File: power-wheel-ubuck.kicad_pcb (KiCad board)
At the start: 2 copper layers, 23 parts, among them J1 CONN_01X02_MALE, J10 TEST_1P, J2 TEST_1P, J3 TEST_1P, J4 CONN_01X03_MALE, J5 TEST_1P, J6 TEST_1P, J7 TEST_1P, J8 TEST_1P, J9 CONN_01X02_MALE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

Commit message: Initial layout start
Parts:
- removed J10: TEST_1P, Measurement_Points:Measurement_Point_Square-SMD-Pad_Big
- moved C2 42.4 mm to (137.2, 90.2)
- moved J5 36.1 mm to (195.2, 110.6)
- moved J6 36.1 mm to (188.7, 110.6)
- moved R2 36.1 mm to (207.5, 114.9)
- moved J2 30.7 mm to (130.8, 81.3)
- moved C3 30.0 mm to (137.2, 94.0)
- moved C1 28.1 mm to (137.2, 86.4)
- moved J8 24.8 mm to (161.3, 81.3)
- moved C6 22.2 mm to (154.9, 90.2)
- moved J3 19.1 mm to (143.5, 81.3)
- moved C5 16.6 mm to (154.9, 94.0)
- moved R1 16.6 mm to (188.1, 101.3)
- moved C7 14.2 mm to (154.9, 86.4)
- moved J4 13.5 mm to (143.5, 107.3), turned to 180 degrees
- moved C4 12.8 mm to (156.4, 124.6)
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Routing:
- net Net-(C1-Pad1): track 0.00 -> 28.8 mm
- net GND: track 0.00 -> 21.6 mm
- added copper zone on F.Cu, net GND
- added copper zone on F.Cu, net Net-(C1-Pad1)
- added copper zone on F.Cu, net Net-(C5-Pad2)

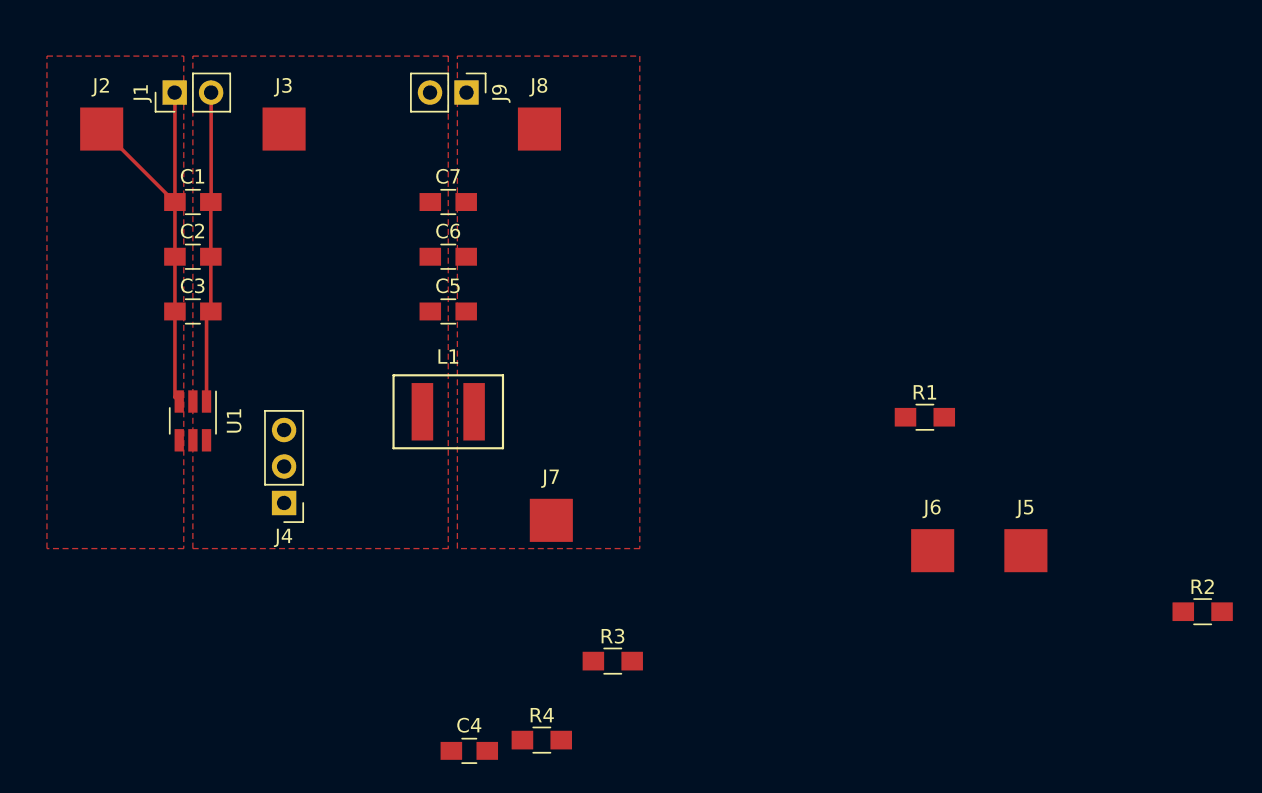
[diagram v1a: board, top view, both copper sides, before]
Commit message: First attempt at layout, needs tightening up
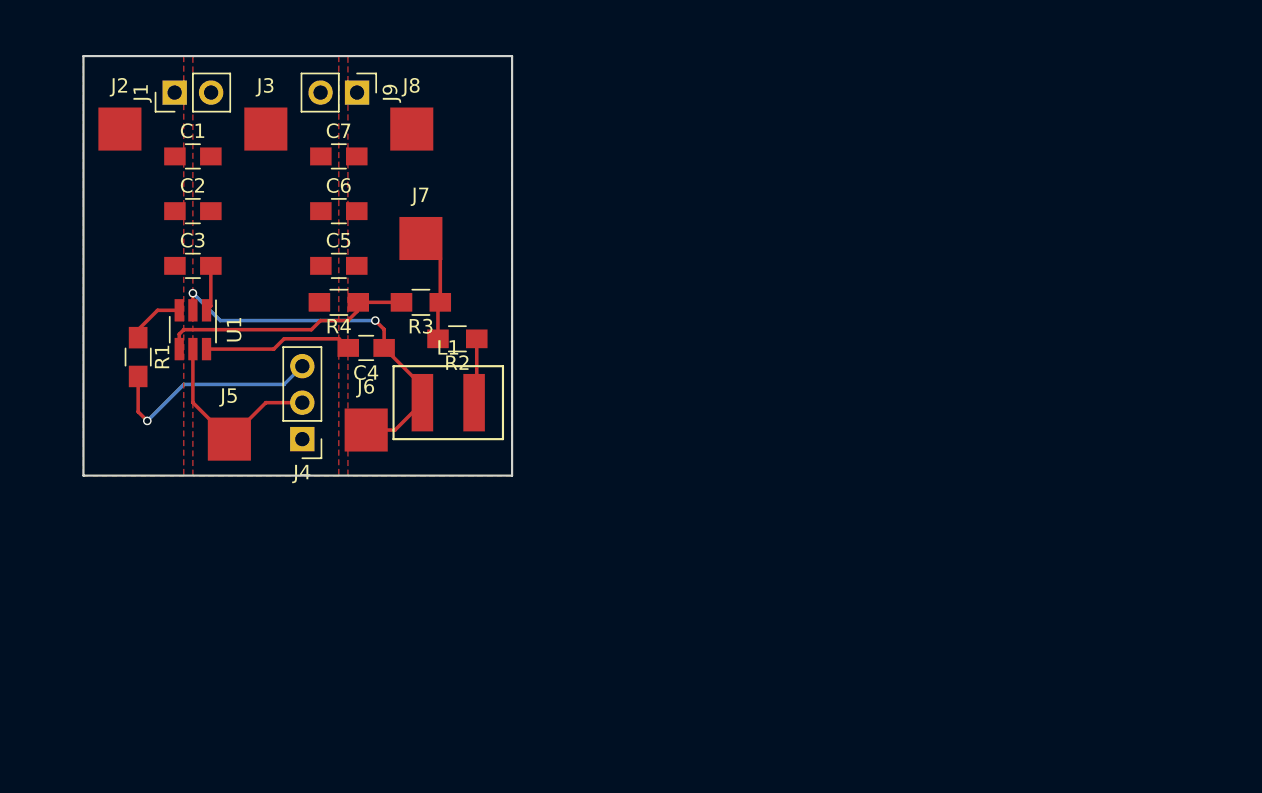
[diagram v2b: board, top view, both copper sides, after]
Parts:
- moved J5 56.0 mm to (139.7, 102.9)
- moved R2 55.3 mm to (155.6, 95.9), turned to 180 degrees
- moved R1 54.9 mm to (133.3, 97.2), turned to 270 degrees
- moved J6 40.3 mm to (149.2, 102.2)
- moved R4 33.6 mm to (147.3, 93.3), turned to 180 degrees
- moved C4 29.0 mm to (149.2, 96.5), turned to 180 degrees
- moved R3 28.3 mm to (153.0, 93.3), turned to 180 degrees
- moved J7 21.6 mm to (153.0, 88.9)
- moved J8 8.89 mm to (152.4, 81.3)
- moved C5 8.26 mm to (147.3, 90.8)
- moved C6 8.26 mm to (147.3, 87.0)
- moved C7 8.26 mm to (147.3, 83.2)
- moved J9 7.62 mm to (148.6, 78.7)
- moved U1 6.35 mm to (137.2, 95.2)
- moved J4 4.62 mm to (144.8, 102.9)
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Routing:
- net Net-(C4-Pad1): track 0.00 -> 26.5 mm, vias 0 -> 2
- net Net-(C1-Pad1): track 28.8 -> 4.02 mm
- net GND: track 21.6 -> 3.25 mm
- net Net-(R3-Pad2): track 0.00 -> 17.7 mm
- net Net-(J4-Pad3): track 0.00 -> 15.7 mm, vias 0 -> 1
- net Net-(J4-Pad2): track 0.00 -> 13.5 mm
- net Net-(C4-Pad2): track 0.00 -> 10.4 mm
- net Net-(J7-Pad1): track 0.00 -> 7.61 mm
- net Net-(C5-Pad2): track 0.00 -> 4.52 mm
- added copper zone on B.Cu, net GND
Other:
- board outline added: 29.8 x 29.2 mm

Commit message: Smaller test pad points
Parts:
- J2, J3, J5, J6, J7, J8: footprint Measurement_Points:Measurement_Point_Square-SMD-Pad_Big -> Measurement_Points:Measurement_Point_Square-SMD-Pad_Small

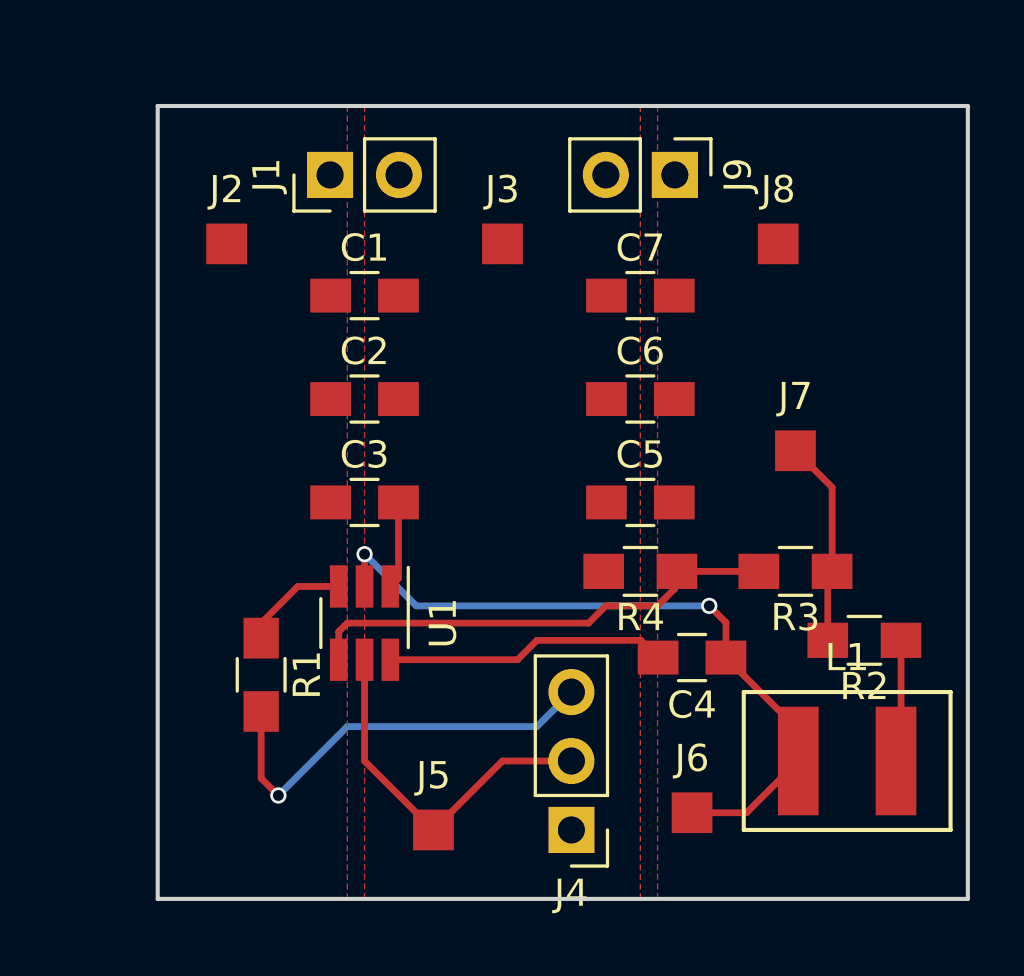
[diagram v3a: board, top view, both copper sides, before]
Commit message: Tightened up the layout
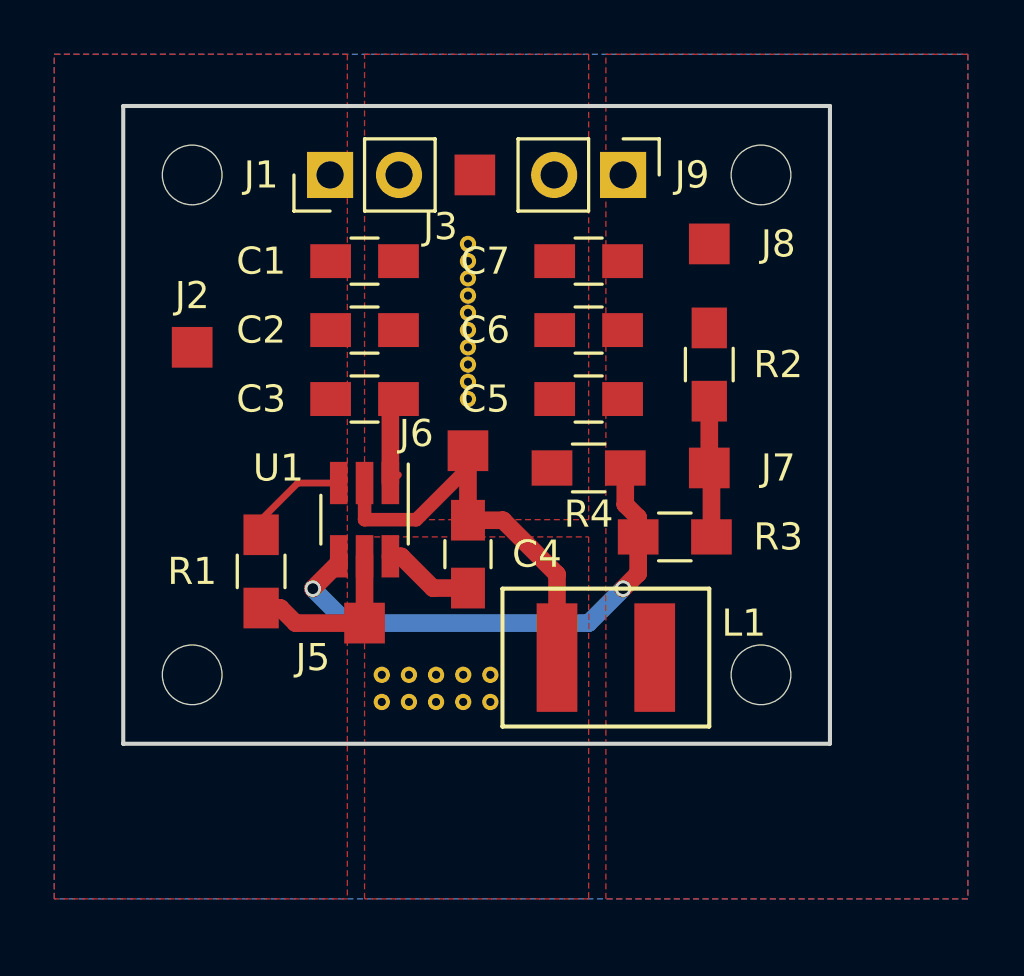
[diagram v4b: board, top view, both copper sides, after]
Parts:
- removed J4: CONN_01X03_MALE, Pin_Headers:Pin_Header_Straight_1x03_Pitch2.54mm
- added REF**: MountingHole_2.2mm_M2, Mounting_Holes:MountingHole_2.2mm_M2, F.Cu at (151.8, 97.2)
- added REF**: VIA-0.6mm, Extras:VIA-0.6mm, F.Cu at (141.0, 83.2)
- added REF**: VIA-0.6mm, Extras:VIA-0.6mm, F.Cu at (141.0, 82.5)
- added REF**: VIA-0.6mm, Extras:VIA-0.6mm, F.Cu at (141.0, 81.9)
- added REF**: VIA-0.6mm, Extras:VIA-0.6mm, F.Cu at (141.0, 81.3)
- added REF**: VIA-0.6mm, Extras:VIA-0.6mm, F.Cu at (141.8, 98.2)
- added REF**: VIA-0.6mm, Extras:VIA-0.6mm, F.Cu at (140.8, 98.2)
- added REF**: VIA-0.6mm, Extras:VIA-0.6mm, F.Cu at (139.8, 98.2)
- added REF**: VIA-0.6mm, Extras:VIA-0.6mm, F.Cu at (138.8, 98.2)
- added REF**: VIA-0.6mm, Extras:VIA-0.6mm, F.Cu at (137.8, 98.2)
- added REF**: VIA-0.6mm, Extras:VIA-0.6mm, F.Cu at (141.8, 97.2)
- added REF**: MountingHole_2.2mm_M2, Mounting_Holes:MountingHole_2.2mm_M2, F.Cu at (130.8, 97.2)
- added REF**: VIA-0.6mm, Extras:VIA-0.6mm, F.Cu at (140.8, 97.2)
- added REF**: VIA-0.6mm, Extras:VIA-0.6mm, F.Cu at (139.8, 97.2)
- added REF**: VIA-0.6mm, Extras:VIA-0.6mm, F.Cu at (138.8, 97.2)
- added REF**: VIA-0.6mm, Extras:VIA-0.6mm, F.Cu at (137.8, 97.2)
- added REF**: MountingHole_2.2mm_M2, Mounting_Holes:MountingHole_2.2mm_M2, F.Cu at (130.8, 78.7)
- added REF**: MountingHole_2.2mm_M2, Mounting_Holes:MountingHole_2.2mm_M2, F.Cu at (151.8, 78.7)
- added REF**: VIA-0.6mm, Extras:VIA-0.6mm, F.Cu at (141.0, 87.0)
- added REF**: VIA-0.6mm, Extras:VIA-0.6mm, F.Cu at (141.0, 86.4)
- added REF**: VIA-0.6mm, Extras:VIA-0.6mm, F.Cu at (141.0, 85.7)
- added REF**: VIA-0.6mm, Extras:VIA-0.6mm, F.Cu at (141.0, 85.1)
- added REF**: VIA-0.6mm, Extras:VIA-0.6mm, F.Cu at (141.0, 84.5)
- added REF**: VIA-0.6mm, Extras:VIA-0.6mm, F.Cu at (141.0, 83.8)
- moved J6 15.7 mm to (141.0, 88.9)
- moved R2 11.7 mm to (149.9, 85.7), turned to 270 degrees
- moved L1 9.67 mm to (146.1, 96.5)
- moved C4 9.09 mm to (141.0, 92.7), turned to 270 degrees
- moved J5 8.03 mm to (137.2, 95.2)
- moved R3 4.62 mm to (148.6, 92.1)
- moved C5 4.26 mm to (145.4, 87.0)
- moved R4 4.26 mm to (145.4, 89.5)
- moved J2 4.02 mm to (130.8, 85.1)
- moved C3 3.81 mm to (137.2, 87.0)
- moved R1 3.81 mm to (133.3, 93.3)
- moved U1 3.81 mm to (137.2, 91.4)
- moved J7 3.24 mm to (149.9, 89.5)
- moved C6 3.18 mm to (145.4, 84.5)
- moved J3 2.74 mm to (141.2, 78.7)
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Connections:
- J5 pad 1: Net-(J4-Pad2) -> Net-(J5-Pad1)
- R1 pad 2: Net-(J4-Pad3) -> Net-(J5-Pad1)
- U1 pad 5: Net-(J4-Pad2) -> Net-(J5-Pad1)
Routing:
- net Net-(J4-Pad3): track 15.7 -> 0.00 mm, vias 1 -> 0
- net Net-(J4-Pad2): track 13.5 -> 0.00 mm
- net Net-(C4-Pad1): track 26.5 -> 16.3 mm, vias 2 -> 0
- net Net-(C4-Pad2): track 10.4 -> 3.34 mm
- net Net-(J5-Pad1): track 0.00 -> 6.50 mm
- net Net-(C5-Pad2): track 4.52 -> 0.00 mm
- net Net-(J7-Pad1): track 7.61 -> 5.03 mm
- net Net-(R3-Pad2): track 17.7 -> 18.9 mm, vias 0 -> 2
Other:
- board size 29.8 x 29.2 mm -> 26 x 23.5 mm
- rule pad_to_mask_clearance: 0.2 -> 0

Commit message: Add some text on the back of the board
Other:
- board text added: "Stephen Legge [ A Legge Up ] Power Wheel μBuck Rev A"
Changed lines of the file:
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@@
     (links 52)
     (no_connects 0)
-    (area 128.194999 76.124999 154.380001 99.770001)
+    (area 121.252857 71.468571 161.322143 105.410001)
     (thickness 1.6)
-    (drawings 4)
+    (drawings 5)
     (tracks 39)
     (zones 0)
@@
   )
   (setup
-    (last_trace_width 0.65)
+    (last_trace_width 0.25)
     (user_trace_width 0.3)
     (user_trace_width 0.35)
@@
     (pad 1 np_thru_hole circle (at 0 0) (size 2.2 2.2) (drill 2.2) (layers *.Cu *.Mask))
   )
+  (gr_text "Stephen Legge\n[ A Legge Up ]\n\nPower Wheel μBuck\n\nRev A" (at 140.97 88.265) (layer B.SilkS)
+    (effects (font (size 1.5 1.5) (thickness 0.3)) (justify mirror))
+  )
   (gr_line (start 128.27 99.695) (end 128.27 76.2) (angle 90) (layer Edge.Cuts) (width 0.15))
   (gr_line (start 154.305 99.695) (end 128.27 99.695) (angle 90) (layer Edge.Cuts) (width 0.15))
@@
   (segment (start 146.765 90.885) (end 146.765 89.535) (width 0.65) (layer F.Cu) (net 7))
   (segment (start 147.24 91.36) (end 146.765 90.885) (width 0.65) (layer F.Cu) (net 7))
-  (segment (start 137.16 92.79) (end 137.16 95.25) (width 0.65) (layer F.Cu) (net 8) (status C00000))
-  (segment (start 133.35 94.695) (end 134.065 94.695) (width 0.65) (layer F.Cu) (net 8) (status 400000))
+  (segment (start 137.16 92.79) (end 137.16 95.25) (width 0.65) (layer F.Cu) (net 8))
+  (segment (start 133.35 94.695) (end 134.065 94.695) (width 0.65) (layer F.Cu) (net 8))
   (segment (start 134.065 94.695) (end 134.62 95.25) (width 0.65) (layer F.Cu) (net 8))
-  (segment (start 134.62 95.25) (end 137.16 95.25) (width 0.65) (layer F.Cu) (net 8) (status 800000))
+  (segment (start 134.62 95.25) (end 137.16 95.25) (width 0.65) (layer F.Cu) (net 8))
   (zone (net 1) (net_name "Net-(C1-Pad1)") (layer F.Cu) (hatch edge 0.508)
     (connect_pads (clearance 0.508))

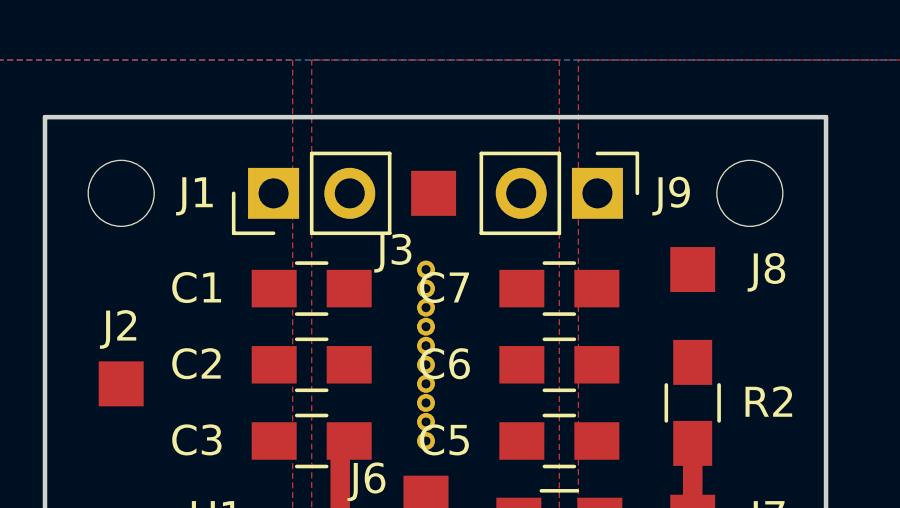
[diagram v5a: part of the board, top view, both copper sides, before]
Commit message: Add some in and out indicators
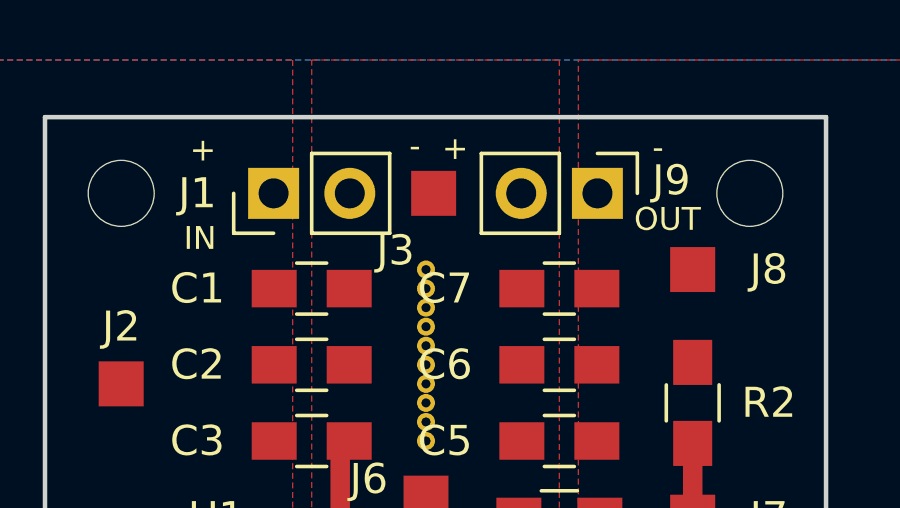
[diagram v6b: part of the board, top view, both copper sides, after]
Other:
- board text added: "+"
- board text added: "-"
- board text added: "IN"
- board text added: "OUT"
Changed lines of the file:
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@@
     (links 52)
     (no_connects 0)
-    (area 121.252857 71.468571 161.322143 105.410001)
+    (area 128.194999 76.124999 154.380001 99.770001)
     (thickness 1.6)
-    (drawings 5)
+    (drawings 11)
     (tracks 39)
     (zones 0)
@@
     (descr "Through hole straight pin header, 1x02, 2.54mm pitch, single row")
     (tags "Through hole pin header THT 1x02 2.54mm single row")
-    (fp_text reference J9 (at 0 -2.54 360) (layer F.SilkS)
+    (fp_text reference J9 (at -0.4318 -2.4638 360) (layer F.SilkS)
       (effects (font (size 1 1) (thickness 0.15)))
     )
@@
     (fp_line (start 1.8 4.35) (end 1.8 -1.8) (layer F.CrtYd) (width 0.05))
     (fp_line (start 1.8 -1.8) (end -1.8 -1.8) (layer F.CrtYd) (width 0.05))
-    (fp_text user %R (at 0 -2.54 360) (layer F.Fab)
+    (fp_text user %R (at -0.4318 -2.4892 360) (layer F.Fab)
       (effects (font (size 1 1) (thickness 0.15)))
     )
@@
     (pad 1 np_thru_hole circle (at 0 0) (size 2.2 2.2) (drill 2.2) (layers *.Cu *.Mask))
   )
+  (gr_text OUT (at 147.9042 79.6036) (layer F.SilkS)
+    (effects (font (size 0.762 0.762) (thickness 0.1905)) (justify left))
+  )
+  (gr_text IN (at 132.8928 80.2386) (layer F.SilkS)
+    (effects (font (size 0.762 0.762) (thickness 0.1905)) (justify left))
+  )
+  (gr_text - (at 148.5138 77.216) (layer F.SilkS)
+    (effects (font (size 0.762 0.762) (thickness 0.1905)) (justify left))
+  )
+  (gr_text + (at 141.5034 77.2414) (layer F.SilkS)
+    (effects (font (size 0.762 0.762) (thickness 0.1905)) (justify left))
+  )
+  (gr_text - (at 140.4112 77.1652) (layer F.SilkS)
+    (effects (font (size 0.762 0.762) (thickness 0.1905)) (justify left))
+  )
+  (gr_text + (at 133.096 77.2922) (layer F.SilkS)
+    (effects (font (size 0.762 0.762) (thickness 0.1905)) (justify left))
+  )
   (gr_text "Stephen Legge\n[ A Legge Up ]\n\nPower Wheel μBuck\n\nRev A" (at 140.97 88.265) (layer B.SilkS)
